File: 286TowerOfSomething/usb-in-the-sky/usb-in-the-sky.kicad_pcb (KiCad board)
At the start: 2 copper layers, 126.5 x 65.9 mm, 36 parts, among them J1 Bus_ISA_8bit, J2 DB25F, SW1 SW_DIP_x07, U1 ST78C36ACJ44, U2 74LS688, Y1 24 MHz

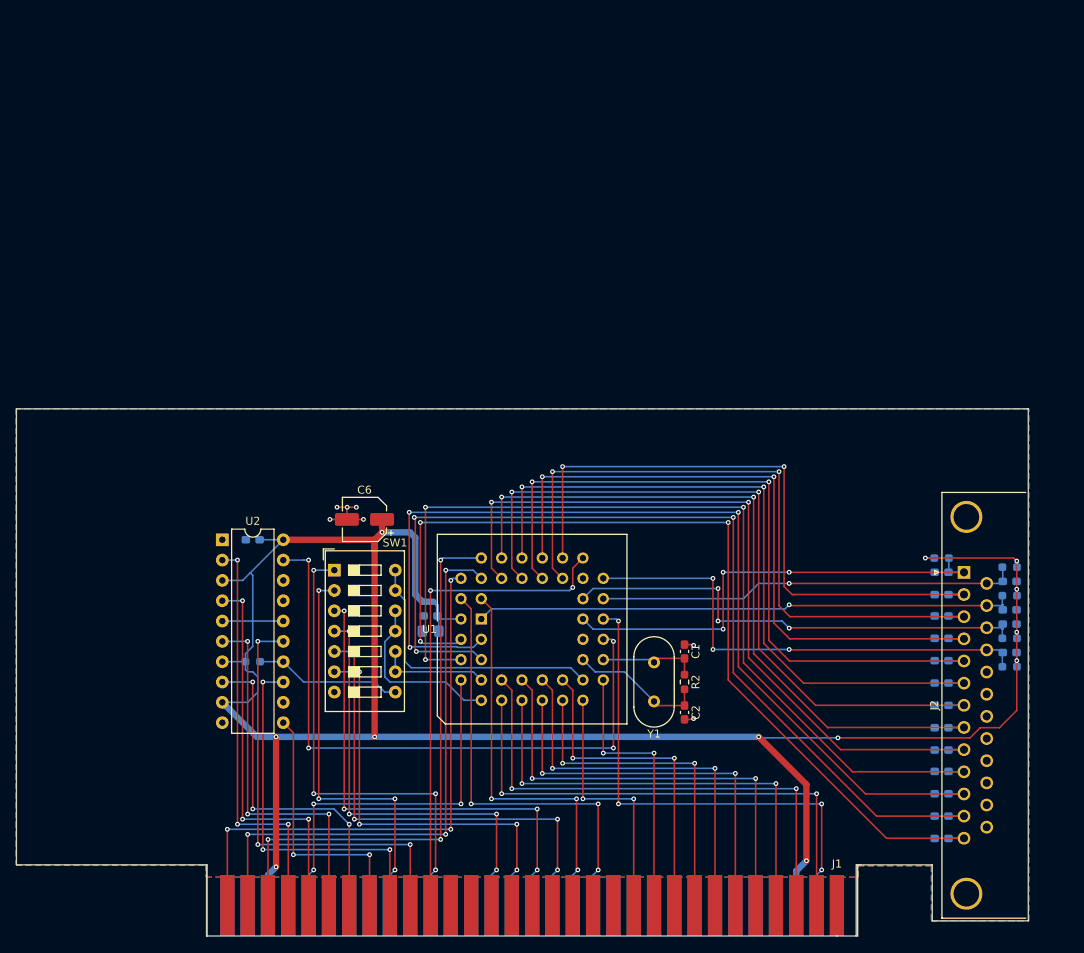
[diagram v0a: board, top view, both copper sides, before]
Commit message: Adding footprints to everything in usb-in-the-sky
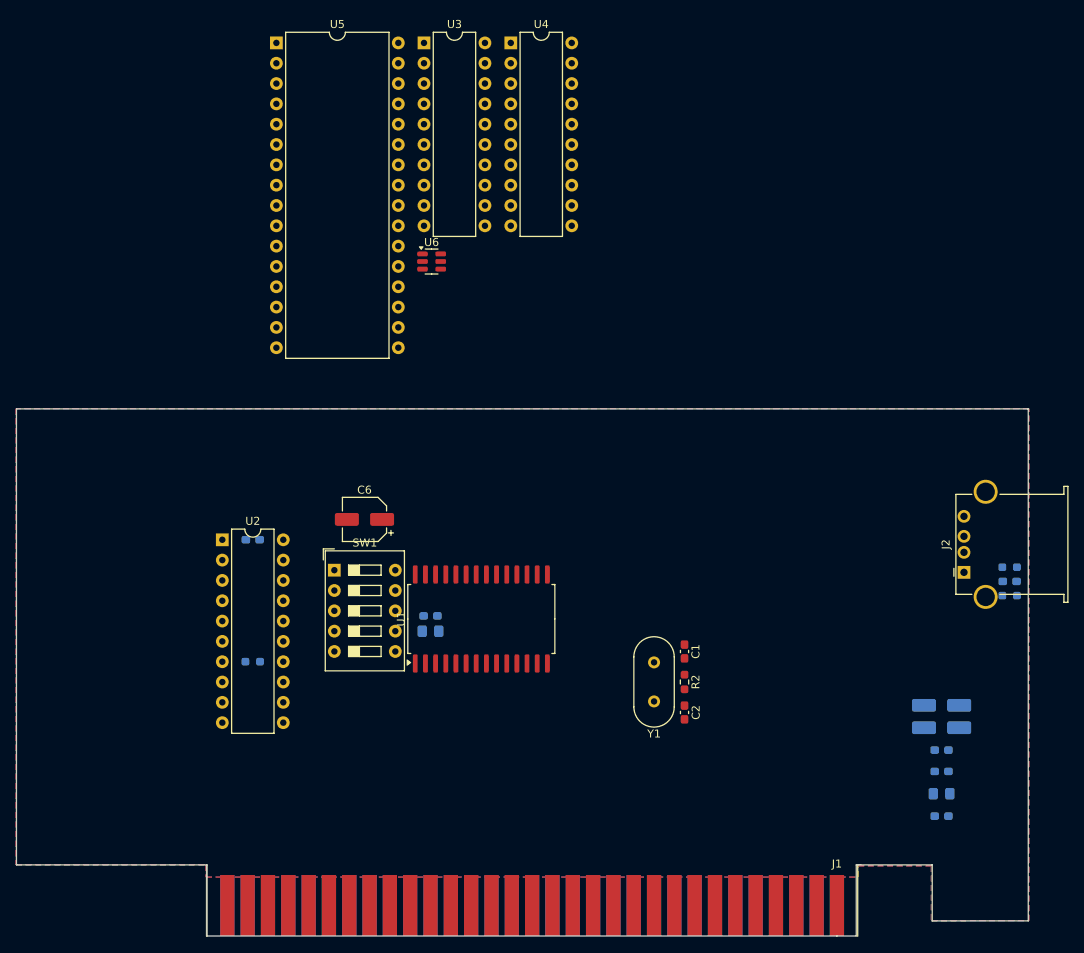
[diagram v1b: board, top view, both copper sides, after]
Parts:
- removed C14, C15, C16, C17, C18, C19, C20, C21, C22, C23: 180p, Capacitor_SMD:C_0603_1608Metric_Pad1.08x0.95mm_HandSolder
- removed R5, R6, R7: 4.7K, Resistor_SMD:R_0603_1608Metric_Pad0.98x0.95mm_HandSolder
- added U3: 74LS245, Package_DIP:DIP-20_W7.62mm, F.Cu at (110.9, 24.3)
- added U4: 74ALS688, Package_DIP:DIP-20_W7.62mm, F.Cu at (121.8, 24.3)
- added U5: SST39SF010, Package_DIP:DIP-32_W15.24mm, F.Cu at (92.5, 24.3)
- added U6: USBLC6-2SC6, Package_TO_SOT_SMD:SOT-23-6, F.Cu at (111.9, 51.6)
- C1, C2: value 22p -> 15p
- C10, C11, C7, C8: value 180p -> 100n
- C12, C13: value 180p -> 100u; footprint Capacitor_SMD:C_0603_1608Metric_Pad1.08x0.95mm_HandSolder -> Capacitor_SMD:CP_Elec_5x5.3
- C9: value 180p -> 1u; footprint Capacitor_SMD:C_0603_1608Metric_Pad1.08x0.95mm_HandSolder -> Capacitor_SMD:C_0805_2012Metric_Pad1.18x1.45mm_HandSolder
- J2: value DB25F -> USB_A; footprint Connector_Dsub:DSUB-25_Female_Horizontal_P2.77x2.84mm_EdgePinOffset4.94mm_Housed_MountingHolesOffset7.48mm -> Connector_USB:USB_A_Stewart_SS-52100-001_Horizontal
- R1: value 10K -> 22
- R2: value 1M -> 22
- R3: value 4.7K -> 10K
- R4: value 4.7K -> 2
- SW1: value SW_DIP_x07 -> SW_DIP_x05; footprint Button_Switch_THT:SW_DIP_SPSTx07_Slide_9.78x19.96mm_W7.62mm_P2.54mm -> Button_Switch_THT:SW_DIP_SPSTx05_Slide_9.78x14.88mm_W7.62mm_P2.54mm
- U1: value ST78C36ACJ44 -> CH375; footprint Package_LCC:PLCC-44_THT-Socket -> Package_SO:SOP-28_8.4x18.16mm_P1.27mm
- Y1: value 24 MHz -> 12 MHz
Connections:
- net /~{LPT_DACK} renamed /A0_CFG
- C1 pad 1: Net-(U1-CLOCK/XTAL1) -> Net-(U1-XI)
- C10 pad 1: Net-(U1-~{ACK}) -> +5V
- C11 pad 1: Net-(U1-PD7) -> +5V
- C12 pad 1: Net-(U1-PD6) -> +5V
- C13 pad 1: Net-(U1-PD5) -> Net-(J2-VBUS)
- C2 pad 1: Net-(U1-XTAL2) -> Net-(U1-XO)
- C7 pad 1: Net-(J2-P14) -> +5V
- C8 pad 1: Net-(U1-PE) -> Net-(U1-V3)
- C9 pad 1: Net-(U1-BUSY) -> Net-(U1-V3)
- J1 pad 43: unconnected-(J1-BA19-Pad43) -> /A19
- J1 pad 44: unconnected-(J1-BA18-Pad44) -> /A18
- J1 pad 45: unconnected-(J1-BA17-Pad45) -> /A17
- J1 pad 46: unconnected-(J1-BA16-Pad46) -> /A16
- J1 pad 47: unconnected-(J1-BA15-Pad47) -> /A15
- J1 pad 48: unconnected-(J1-BA14-Pad48) -> /A14
- J1 pad 49: unconnected-(J1-BA13-Pad49) -> /A13
- J1 pad 50: unconnected-(J1-BA12-Pad50) -> /A12
- J1 pad 51: unconnected-(J1-BA11-Pad51) -> /A11
- J2 pad 1: Net-(U1-~{STROBE}) -> Net-(J2-VBUS)
- J2 pad 2: Net-(U1-PD0) -> Net-(J2-D-)
- J2 pad 3: Net-(U1-PD1) -> Net-(J2-D+)
- J2 pad 4: Net-(U1-PD2) -> GND
- J2 pad 5: Net-(U1-PD3) -> GND
- R1 pad 1: +5V -> Net-(U1-UD+)
- R1 pad 2: Net-(U2-R5) -> Net-(R1-Pad2)
- R2 pad 1: Net-(U1-XTAL2) -> Net-(U1-UD-)
- R2 pad 2: Net-(U1-CLOCK/XTAL1) -> Net-(R2-Pad2)
- R3 pad 2: Net-(J2-P14) -> Net-(U4-R4)
- R4 pad 2: Net-(J2-P15) -> Net-(J2-VBUS)
- SW1 pad 1: /IRQ7 -> /A0
- SW1 pad 2: /IRQ5 -> /A1
- SW1 pad 3: /DRQ3 -> GND
- SW1 pad 4: /DRQ1 -> GND
- SW1 pad 5: /~{DACK3} -> /~{MEMWR}
- SW1 pad 6: /~{DACK1} -> /~{ROMWE}
- SW1 pad 7: GND -> /SW_ROM_EN
- SW1 pad 8: Net-(U2-R5) -> Net-(U4-R4)
- U1 pad 1: Net-(J2-P15) -> unconnected-(U1-~{INT}-Pad1)
- U1 pad 10: /D6 -> Net-(U1-UD+)
- U1 pad 11: /D5 -> Net-(U1-UD-)
- U1 pad 12: /D4 -> GND
- U1 pad 13: /D3 -> Net-(U1-XI)
- U1 pad 14: /D2 -> Net-(U1-XO)
- U1 pad 15: /D1 -> Net-(U1-D0)
- U1 pad 16: /D0 -> Net-(U1-D1)
- U1 pad 17: /AEN -> Net-(U1-D2)
- U1 pad 18: /IOCHRDY -> Net-(U1-D3)
- U1 pad 19: /LPT_IRQ -> Net-(U1-D4)
- U1 pad 2: Net-(U1-SLCT) -> /RESET
- U1 pad 20: Net-(U1-CLOCK/XTAL1) -> Net-(U1-D5)
- U1 pad 21: Net-(U1-XTAL2) -> Net-(U1-D6)
- U1 pad 22: /~{LPT_CS} -> Net-(U1-D7)
- U1 pad 24: /RESET -> /~{ACT}
- U1 pad 25: Net-(U1-~{STROBE}) -> unconnected-(U1-RST-Pad25)
- U1 pad 26: Net-(J2-P14) -> unconnected-(U1-~{RST}-Pad26)
- U1 pad 27: Net-(J2-P16) -> /~{USB_CS}
- U1 pad 28: Net-(J2-P17) -> +5V
- U1 pad 3: Net-(U1-BUSY) -> /~{IOW}
- U1 pad 4: Net-(U1-~{ACK}) -> /~{IOR}
- U1 pad 5: Net-(U1-PE) -> unconnected-(U1-TXD-Pad5)
- U1 pad 6: /TC -> unconnected-(U1-RXD-Pad6)
- U1 pad 7: /LPT_DRQ -> unconnected-(U1-NC-Pad7)
- U1 pad 9: /D7 -> Net-(U1-V3)
- U2 pad 1: GND -> /AEN
- U2 pad 11: /A7 -> /A6
- U2 pad 12: GND -> +5V
- U2 pad 13: /A8 -> /A5
- U2 pad 14: Net-(U2-R5) -> GND
- U2 pad 15: /A9 -> /A4
- U2 pad 16: +5V -> GND
- U2 pad 17: GND -> /A3
- U2 pad 19: /~{LPT_CS} -> /~{USB_CS}
- U2 pad 2: /A3 -> GND
- U2 pad 3: +5V -> GND
- U2 pad 4: /A4 -> /A9
- U2 pad 6: /A5 -> /A8
- U2 pad 7: +5V -> GND
- U2 pad 8: /A6 -> /A7
- Y1 pad 1: Net-(U1-CLOCK/XTAL1) -> Net-(U1-XI)
- Y1 pad 2: Net-(U1-XTAL2) -> Net-(U1-XO)
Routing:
- net +5V: track 288.8 -> 0.00 mm, vias 12 -> 0
- net Net-(U1-BUSY): track 123.7 -> 0.00 mm, vias 3 -> 0
- net Net-(U1-PE): track 122.9 -> 0.00 mm, vias 3 -> 0
- net Net-(U1-SLCT): track 118.0 -> 0.00 mm, vias 3 -> 0
- net Net-(U1-~{ACK}): track 117.9 -> 0.00 mm, vias 3 -> 0
- net Net-(U1-PD7): track 95.3 -> 0.00 mm, vias 2 -> 0
- net Net-(U1-PD5): track 92.3 -> 0.00 mm, vias 2 -> 0
- net Net-(U1-PD6): track 90.8 -> 0.00 mm, vias 2 -> 0
- net Net-(U1-PD3): track 89.4 -> 0.00 mm, vias 2 -> 0
- net Net-(U1-PD4): track 87.7 -> 0.00 mm, vias 2 -> 0
- net Net-(U1-PD1): track 84.6 -> 0.00 mm, vias 2 -> 0
- net Net-(U1-PD2): track 83.9 -> 0.00 mm, vias 2 -> 0
- net /~{LPT_CS}: track 79.5 -> 0.00 mm, vias 4 -> 0
- net Net-(U1-PD0): track 79.0 -> 0.00 mm, vias 2 -> 0
- net /A1: track 71.5 -> 0.00 mm, vias 3 -> 0
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
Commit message: Started working on usb-in-the-sky layout
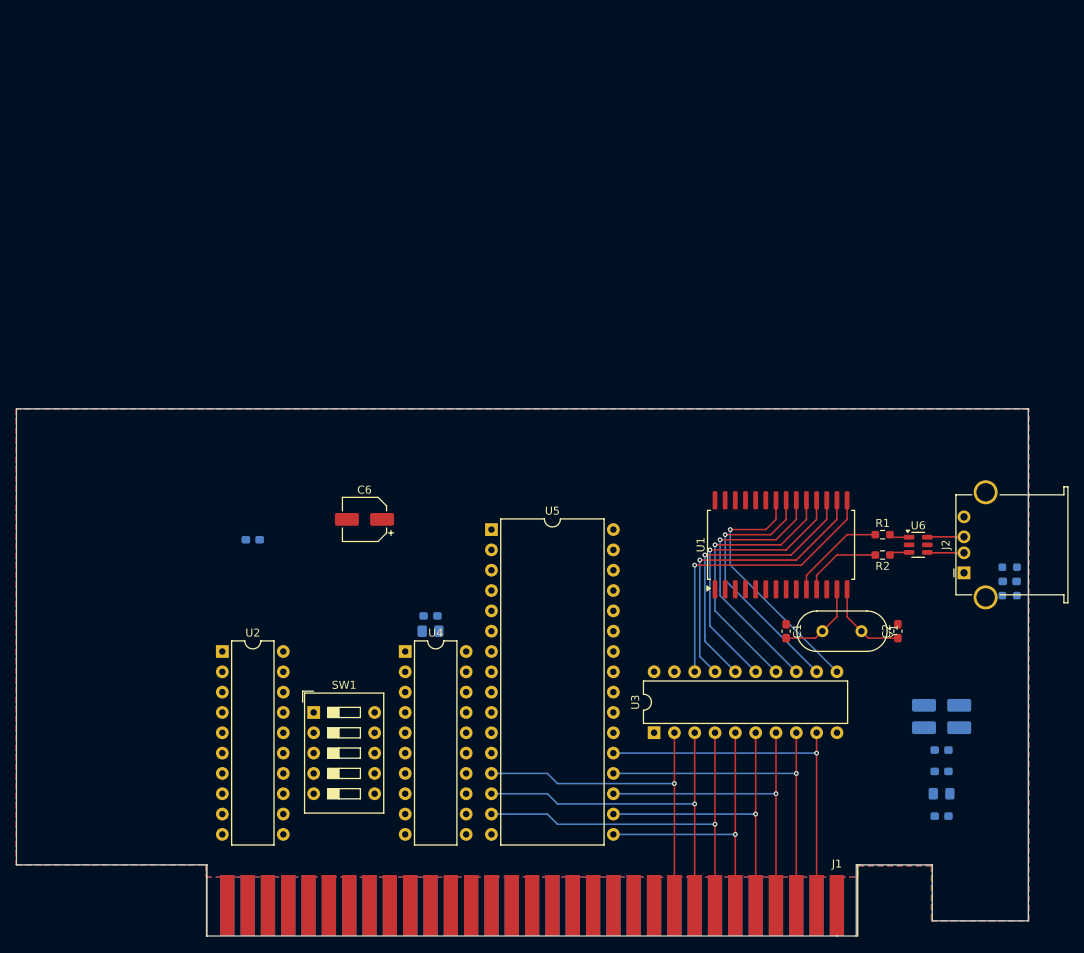
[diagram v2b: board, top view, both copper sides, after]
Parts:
- R1: moved to F.Cu
- moved U3 90.9 mm to (139.7, 110.5), turned to 90 degrees
- moved R1 80.3 mm to (168.3, 85.7)
- moved U4 77.2 mm to (108.6, 100.3)
- moved U6 70.4 mm to (172.7, 87.0)
- moved U5 66.5 mm to (119.4, 85.1)
- moved U1 38.6 mm to (155.6, 87.0)
- moved R2 29.4 mm to (168.3, 88.3), turned to 0 degrees
- moved C2 28.5 mm to (170.2, 97.8), turned to 90 degrees
- moved Y1 21.4 mm to (160.7, 97.8), turned to 0 degrees
- moved SW1 18.0 mm to (97.2, 108.0)
- moved U2 14.0 mm to (85.7, 100.3)
- moved C1 13.0 mm to (156.2, 97.8)
- moved J2 0.06 mm to (178.4, 90.5)
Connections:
- U6 pad 1: Net-(J2-D+) -> Net-(R1-Pad2)
- U6 pad 3: Net-(J2-D-) -> Net-(R2-Pad2)
- U6 pad 4: Net-(R2-Pad2) -> Net-(J2-D-)
- U6 pad 6: Net-(R1-Pad2) -> Net-(J2-D+)
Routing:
- net /D2: track 0.00 -> 50.1 mm, vias 0 -> 1
- net /D1: track 0.00 -> 47.5 mm, vias 0 -> 1
- net /D7: track 0.00 -> 47.0 mm, vias 0 -> 1
- net /D0: track 0.00 -> 45.0 mm, vias 0 -> 1
- net /D6: track 0.00 -> 44.5 mm, vias 0 -> 1
- net /D5: track 0.00 -> 41.9 mm, vias 0 -> 1
- net /D4: track 0.00 -> 39.4 mm, vias 0 -> 1
- net Net-(U1-D0): track 0.00 -> 37.1 mm, vias 0 -> 1
- net /D3: track 0.00 -> 36.8 mm, vias 0 -> 1
- net Net-(U1-D1): track 0.00 -> 36.4 mm, vias 0 -> 1
- net Net-(U1-D2): track 0.00 -> 35.6 mm, vias 0 -> 1
- net Net-(U1-D3): track 0.00 -> 34.9 mm, vias 0 -> 1
- net Net-(U1-D4): track 0.00 -> 34.2 mm, vias 0 -> 1
- net Net-(U1-D5): track 0.00 -> 33.4 mm, vias 0 -> 1
- net Net-(U1-D6): track 0.00 -> 32.7 mm, vias 0 -> 1
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
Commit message: More layout work on usb-in-the-sky
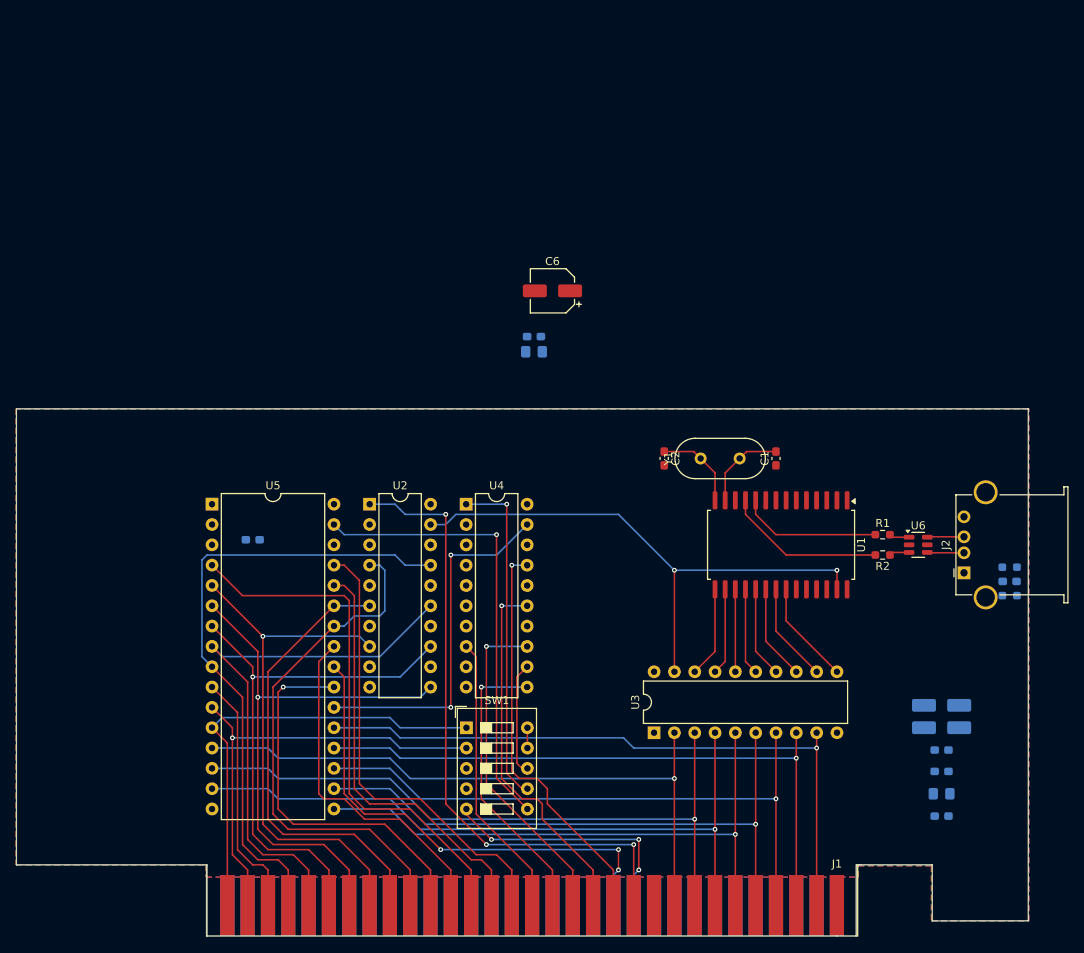
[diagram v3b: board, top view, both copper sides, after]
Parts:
- moved C4 37.2 mm to (124.7, 61.0)
- moved C5 37.2 mm to (124.7, 62.9)
- moved C6 37.0 mm to (127.0, 55.2)
- moved C2 36.3 mm to (141.0, 76.2), turned to -90 degrees
- moved U5 35.1 mm to (84.5, 81.9)
- moved U2 26.0 mm to (104.2, 81.9)
- moved Y1 23.9 mm to (150.4, 76.2), turned to 180 degrees
- moved C1 21.6 mm to (154.9, 76.2), turned to -90 degrees
- moved U4 19.9 mm to (116.2, 81.9)
- moved SW1 19.2 mm to (116.2, 109.9)
- turned U1 to -90 degrees
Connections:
- J1 pad 11: unconnected-(J1-~{SMEMW}-Pad11) -> /~{MEMWR}
- J1 pad 12: unconnected-(J1-~{SMEMR}-Pad12) -> /~{MEMRD}
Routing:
- net /AEN: track 0.00 -> 79.5 mm, vias 0 -> 3
- net /A3: track 0.00 -> 78.5 mm
- net /A6: track 0.00 -> 70.4 mm, vias 0 -> 1
- net /A4: track 0.00 -> 70.1 mm
- net /~{USB_CS}: track 0.00 -> 69.3 mm, vias 0 -> 2
- net /A5: track 0.00 -> 67.8 mm, vias 0 -> 1
- net /A12: track 0.00 -> 66.8 mm
- net /A7: track 0.00 -> 66.5 mm, vias 0 -> 1
- net /A9: track 0.00 -> 65.5 mm
- net /~{MEMRD}: track 0.00 -> 60.8 mm, vias 0 -> 3
- net /A14: track 0.00 -> 57.3 mm
- net /A8: track 0.00 -> 56.9 mm
- net /~{ROMWE}: track 0.00 -> 56.7 mm, vias 0 -> 1
- net /A1: track 0.00 -> 56.4 mm, vias 0 -> 1
- net /A0: track 0.00 -> 55.9 mm
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
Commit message: Layout done?
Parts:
- C10, C11, C12, C13, C3, C4, C5, C7, C8, C9, R3, R4: moved to F.Cu
- moved C10 76.6 mm to (108.0, 79.4)
- moved C11 64.8 mm to (120.0, 79.4)
- moved R3 58.5 mm to (127.0, 102.2)
- moved C3 51.8 mm to (137.2, 106.7), turned to -90 degrees
- moved C5 50.6 mm to (161.9, 97.2), turned to -90 degrees
- moved C8 48.5 mm to (156.8, 76.2), turned to 90 degrees
- moved C9 45.2 mm to (158.8, 76.2), turned to 90 degrees
- moved C4 37.5 mm to (92.1, 79.4)
- moved C6 27.4 mm to (108.0, 74.9)
- moved C7 21.1 mm to (163.8, 97.2), turned to -90 degrees
- moved C12 14.7 mm to (168.3, 97.2), turned to -90 degrees
- moved R4 11.7 mm to (172.7, 90.8), turned to 0 degrees
- moved C13 9.96 mm to (174.6, 97.2), turned to -90 degrees
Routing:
- net +5V: track 0.00 -> 276.5 mm, vias 0 -> 10
- net /~{IOR}: track 0.00 -> 90.8 mm, vias 0 -> 4
- net /~{IOW}: track 0.00 -> 79.5 mm, vias 0 -> 3
- net /A0_CFG: track 2.54 -> 62.0 mm, vias 0 -> 3
- net /RESET: track 0.00 -> 53.3 mm, vias 0 -> 3
- net Net-(J2-VBUS): track 0.00 -> 14.4 mm
- net Net-(U1-V3): track 0.00 -> 10.2 mm
- net /A19: track 51.0 -> 55.9 mm, vias 1 -> 3
- net /A18: track 46.5 -> 50.2 mm, vias 1 -> 3
- net Net-(U4-R4): track 14.2 -> 16.4 mm
- net /A10: track 48.5 -> 47.6 mm
- net /A8: track 56.9 -> 56.0 mm
- net /A9: track 65.5 -> 64.6 mm

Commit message: Shrinking board
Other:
- board size 126.5 x 65.9 mm -> 105.8 x 65.9 mm
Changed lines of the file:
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@@
 	)
 	(gr_line
-		(start 60 127)
-		(end 60 70)
+		(start 80.645 127)
+		(end 80.645 70)
 		(stroke
 			(width 0.05)
@@
 	(gr_line
 		(start 186.47725 70)
-		(end 60 70)
+		(end 80.645 70)
 		(stroke
 			(width 0.05)
@@
 	(gr_line
 		(start 83.82 127)
-		(end 60 127)
+		(end 80.645 127)
 		(stroke
 			(width 0.05)
